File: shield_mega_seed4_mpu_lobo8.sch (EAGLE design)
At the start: 33 parts, among them U1 GY-521MPU6050

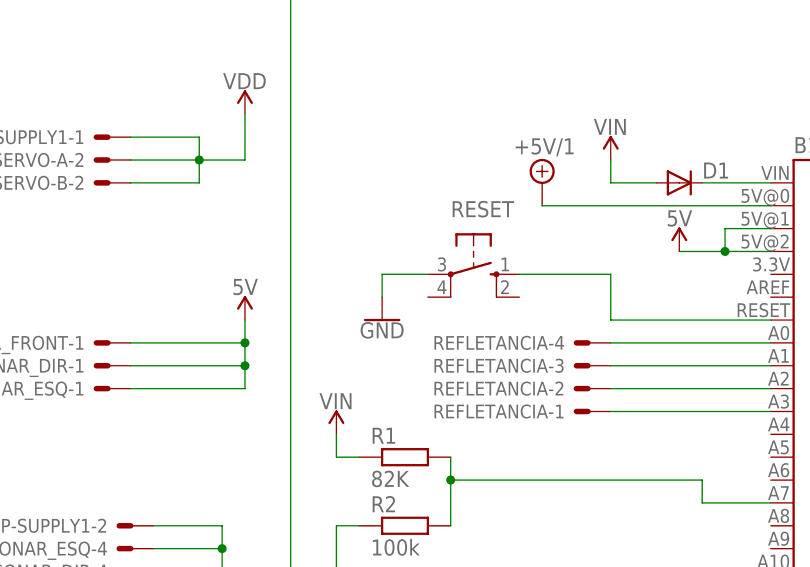
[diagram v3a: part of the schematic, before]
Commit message: Adição de terra em pino do botão de reset que estava faltando
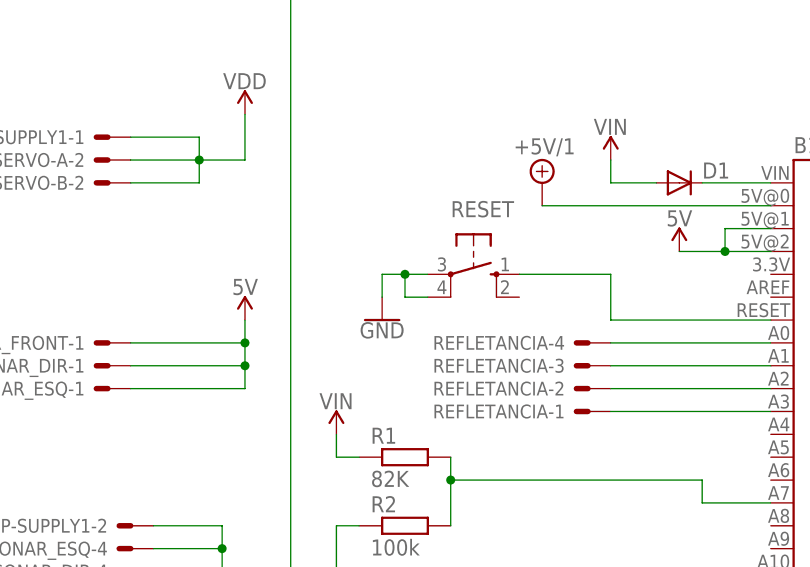
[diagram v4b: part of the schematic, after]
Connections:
- net GND: now also RESET.P1
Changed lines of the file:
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@@
 <segment>
 <pinref part="RESET" gate="1" pin="P"/>
-<wire x1="27.94" y1="86.36" x2="22.86" y2="86.36" width="0.1524" layer="91"/>
+<wire x1="27.94" y1="86.36" x2="25.4" y2="86.36" width="0.1524" layer="91"/>
 <pinref part="GND11" gate="1" pin="GND"/>
+<wire x1="25.4" y1="86.36" x2="22.86" y2="86.36" width="0.1524" layer="91"/>
 <wire x1="22.86" y1="83.82" x2="22.86" y2="86.36" width="0.1524" layer="91"/>
+<pinref part="RESET" gate="1" pin="P1"/>
+<wire x1="27.94" y1="83.82" x2="25.4" y2="83.82" width="0.1524" layer="91"/>
+<wire x1="25.4" y1="83.82" x2="25.4" y2="86.36" width="0.1524" layer="91"/>
+<junction x="25.4" y="86.36"/>
 </segment>
 <segment>

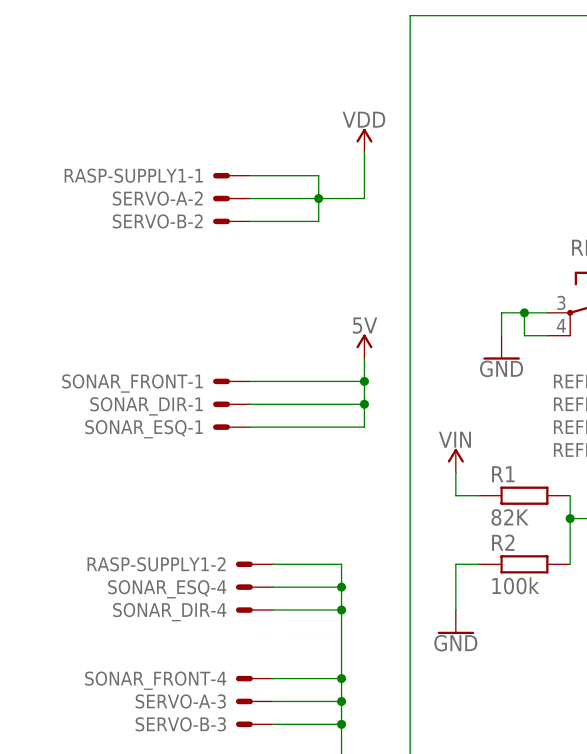
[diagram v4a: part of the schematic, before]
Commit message: Remoção do conector de alimentação do raspberry PI
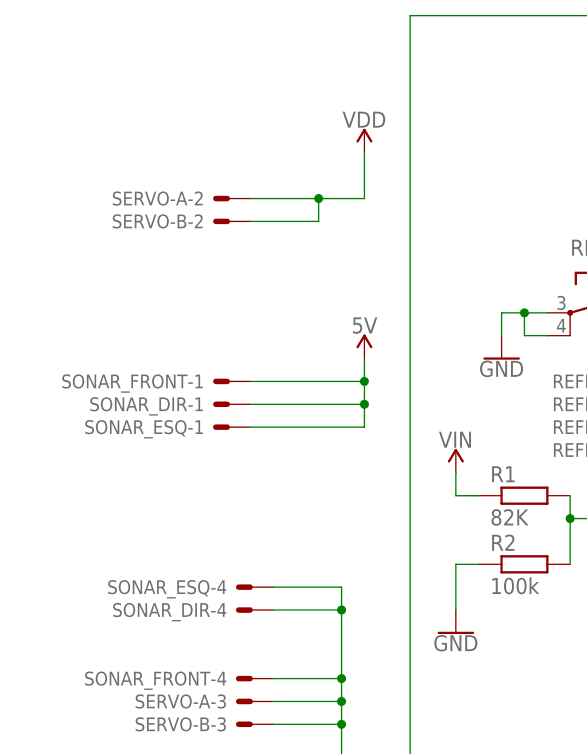
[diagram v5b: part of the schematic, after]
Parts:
- removed RASP-SUPPLY1: 22-23-2021, con-molex:22-23-2021
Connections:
- net GND: no longer RASP-SUPPLY1-2.S
- net VDD: no longer RASP-SUPPLY1-1.S
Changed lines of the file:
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@@
 <part name="SUPPLY6" library="SparkFun-PowerSymbols" deviceset="VDD" device=""/>
 <part name="SUPPLY7" library="SparkFun-PowerSymbols" deviceset="VDD" device=""/>
-<part name="RASP-SUPPLY1" library="con-molex" deviceset="22-23-2021" device="" value=""/>
 <part name="RASP-COM" library="con-molex" deviceset="22-23-2021" device="" value=""/>
 <part name="REFLETANCIA" library="con-molex" deviceset="22-23-2041" device="" value=""/>
@@
 <instance part="SUPPLY6" gate="VDD" x="15.24" y="12.7"/>
 <instance part="SUPPLY7" gate="VDD" x="7.62" y="104.14"/>
-<instance part="RASP-SUPPLY1" gate="-1" x="-7.62" y="101.6" rot="R180"/>
 <instance part="RASP-COM" gate="-1" x="91.44" y="109.22" rot="R180"/>
 <instance part="RASP-COM" gate="-2" x="91.44" y="106.68" rot="R180"/>
@@
 <instance part="SUPPLY5" gate="G$1" x="109.22" y="134.62"/>
 <instance part="GND4" gate="1" x="119.38" y="124.46"/>
-<instance part="RASP-SUPPLY1" gate="-2" x="-5.08" y="58.42" rot="R180"/>
 </instances>
 <busses>
@@
 <wire x1="5.08" y1="55.88" x2="5.08" y2="53.34" width="0.1524" layer="91"/>
 <junction x="5.08" y="53.34"/>
-<pinref part="RASP-SUPPLY1" gate="-2" pin="S"/>
-<wire x1="-2.54" y1="58.42" x2="5.08" y2="58.42" width="0.1524" layer="91"/>
-<wire x1="5.08" y1="58.42" x2="5.08" y2="55.88" width="0.1524" layer="91"/>
-<junction x="5.08" y="55.88"/>
 </segment>
 <segment>
@@
 <wire x1="2.54" y1="99.06" x2="7.62" y2="99.06" width="0.1524" layer="91"/>
 <wire x1="7.62" y1="99.06" x2="7.62" y2="104.14" width="0.1524" layer="91"/>
-<wire x1="2.54" y1="101.6" x2="2.54" y2="99.06" width="0.1524" layer="91"/>
 <pinref part="SERVO-A" gate="-2" pin="S"/>
 <wire x1="-5.08" y1="99.06" x2="2.54" y2="99.06" width="0.1524" layer="91"/>
@@
 <wire x1="2.54" y1="96.52" x2="2.54" y2="99.06" width="0.1524" layer="91"/>
 <wire x1="-5.08" y1="96.52" x2="2.54" y2="96.52" width="0.1524" layer="91"/>
-<pinref part="RASP-SUPPLY1" gate="-1" pin="S"/>
-<wire x1="-5.08" y1="101.6" x2="2.54" y2="101.6" width="0.1524" layer="91"/>
-</segment>
-<segment>
+</segment>
+<segment>

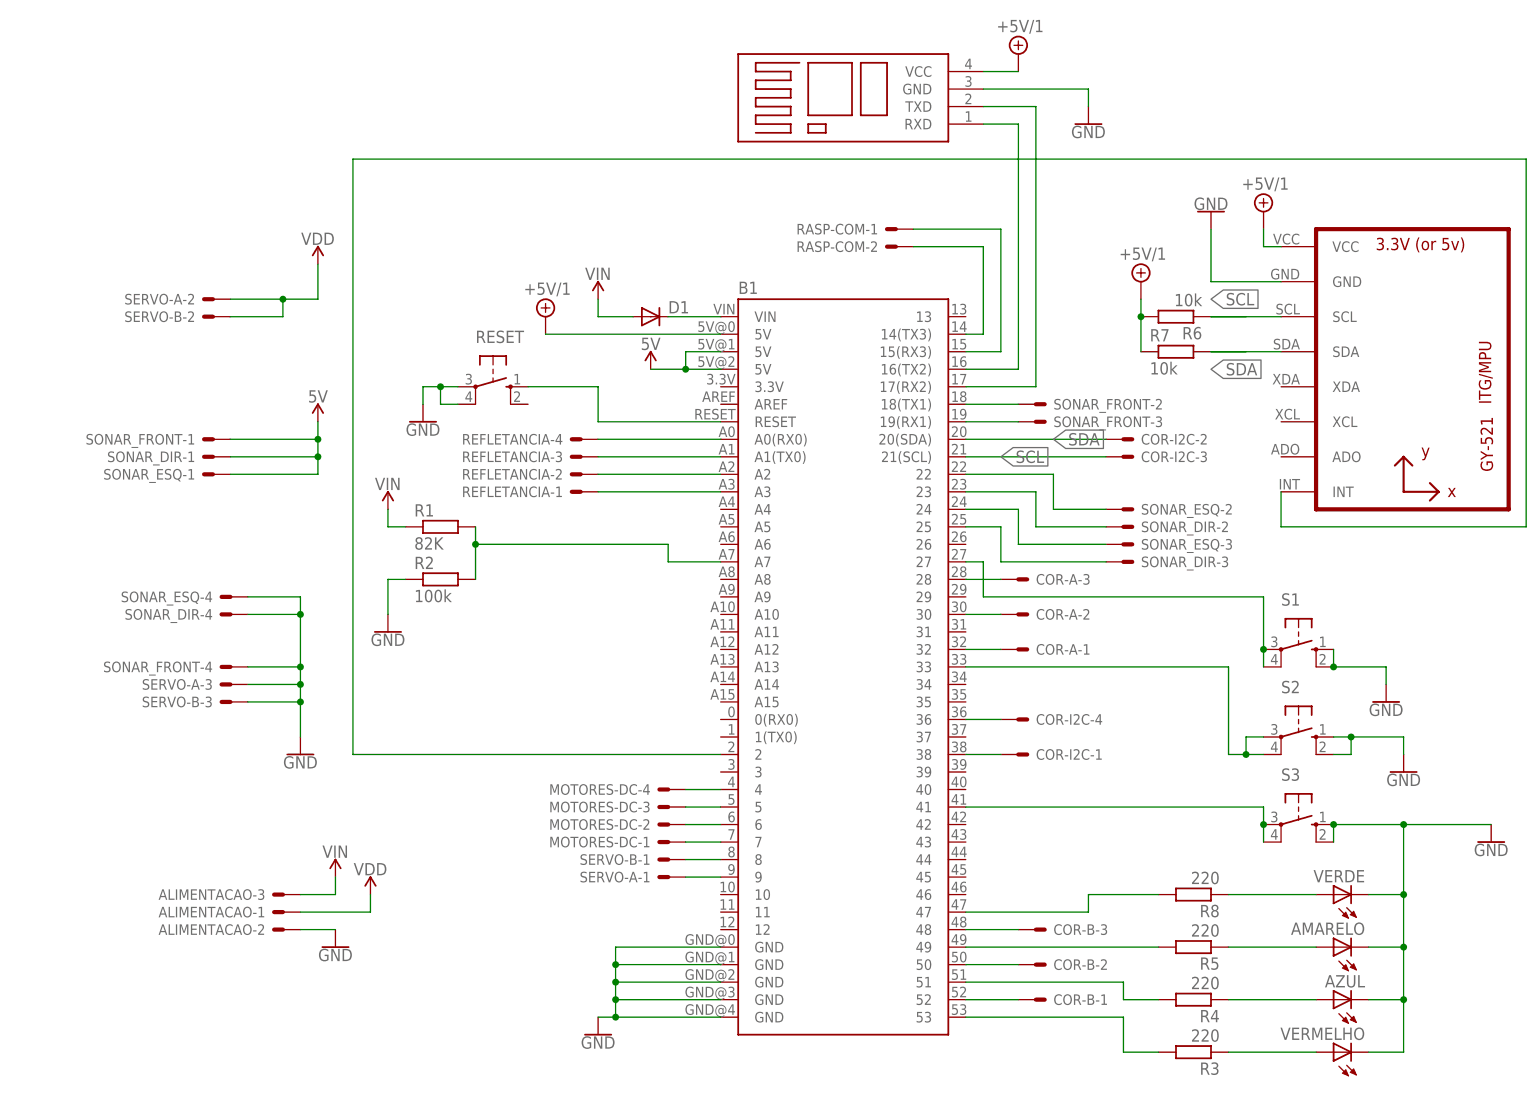
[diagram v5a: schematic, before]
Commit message: Adicionado o conector para o novo modelo da placa.
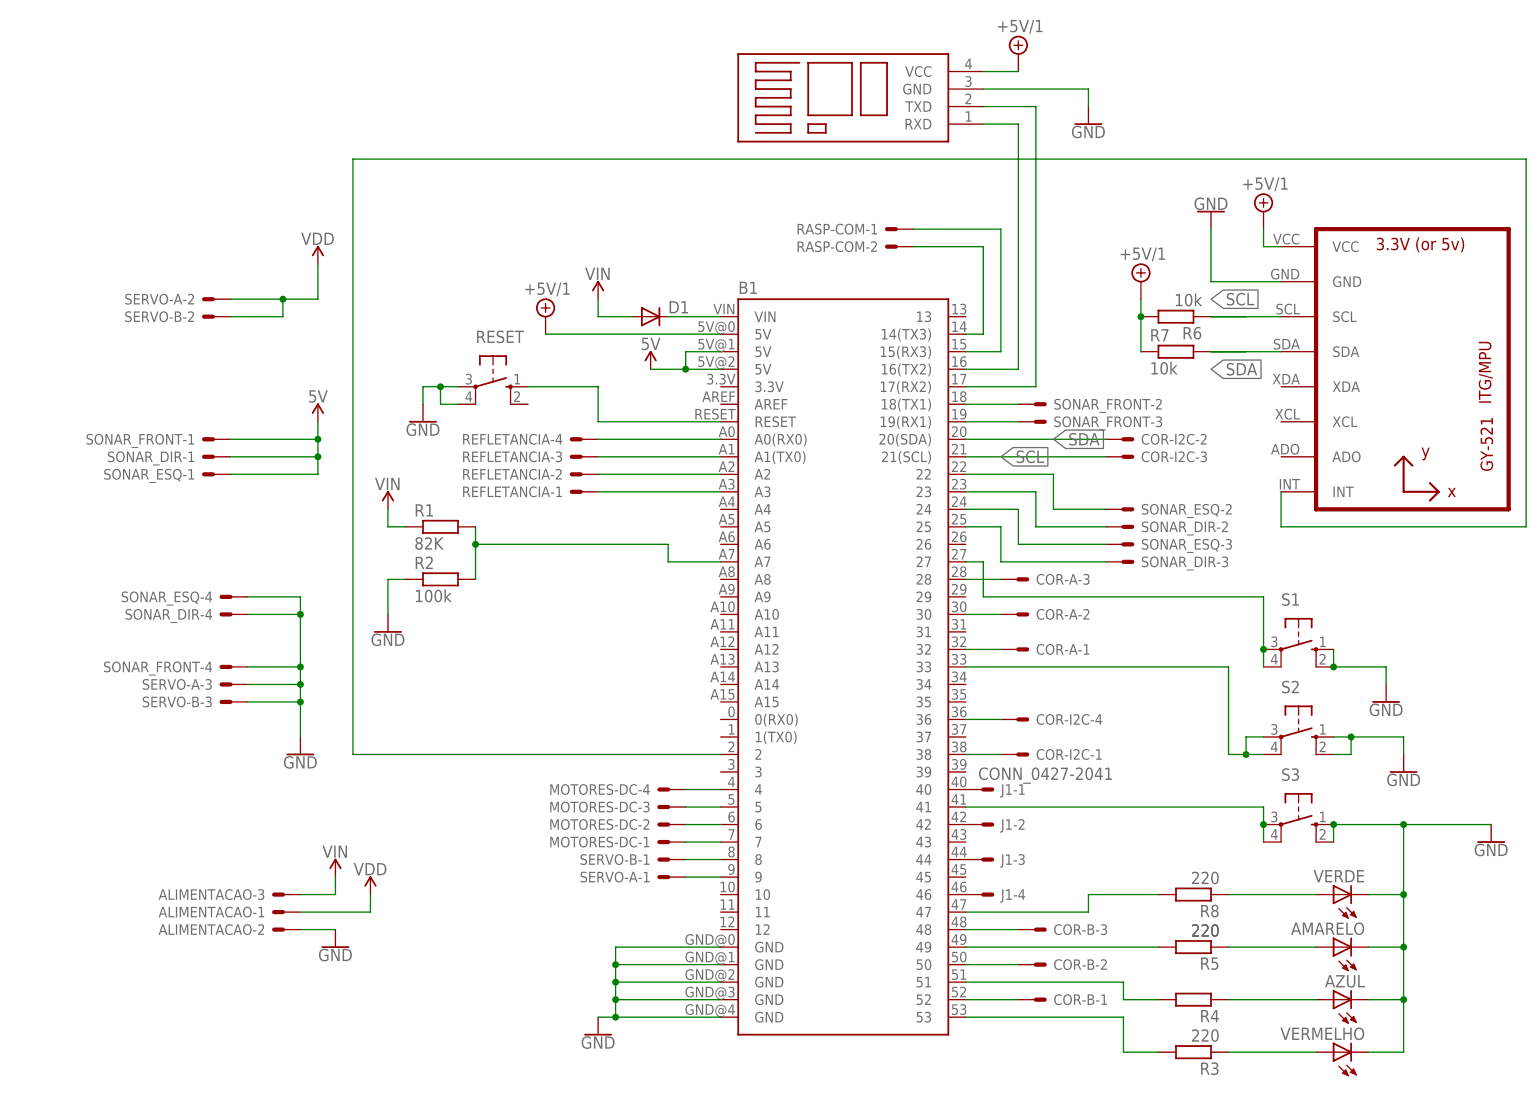
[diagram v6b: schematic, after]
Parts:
- added J1: CONN_0427-2041, Robotica-IFRN-SC-conectores:CONN_0427-2041
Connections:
- new net N$44: B1.40, J1-1.S
- new net N$45: B1.42, J1-2.S
- new net N$46: B1.44, J1-3.S
- new net N$47: B1.46, J1-4.S
